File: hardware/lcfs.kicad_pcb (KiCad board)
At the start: 2 copper layers, 10 parts, among them J1 Pin_1x3, J2 Pin_1x3, J3 Pin_1x2_Battery, J4 Pin_1x3_Transmitter

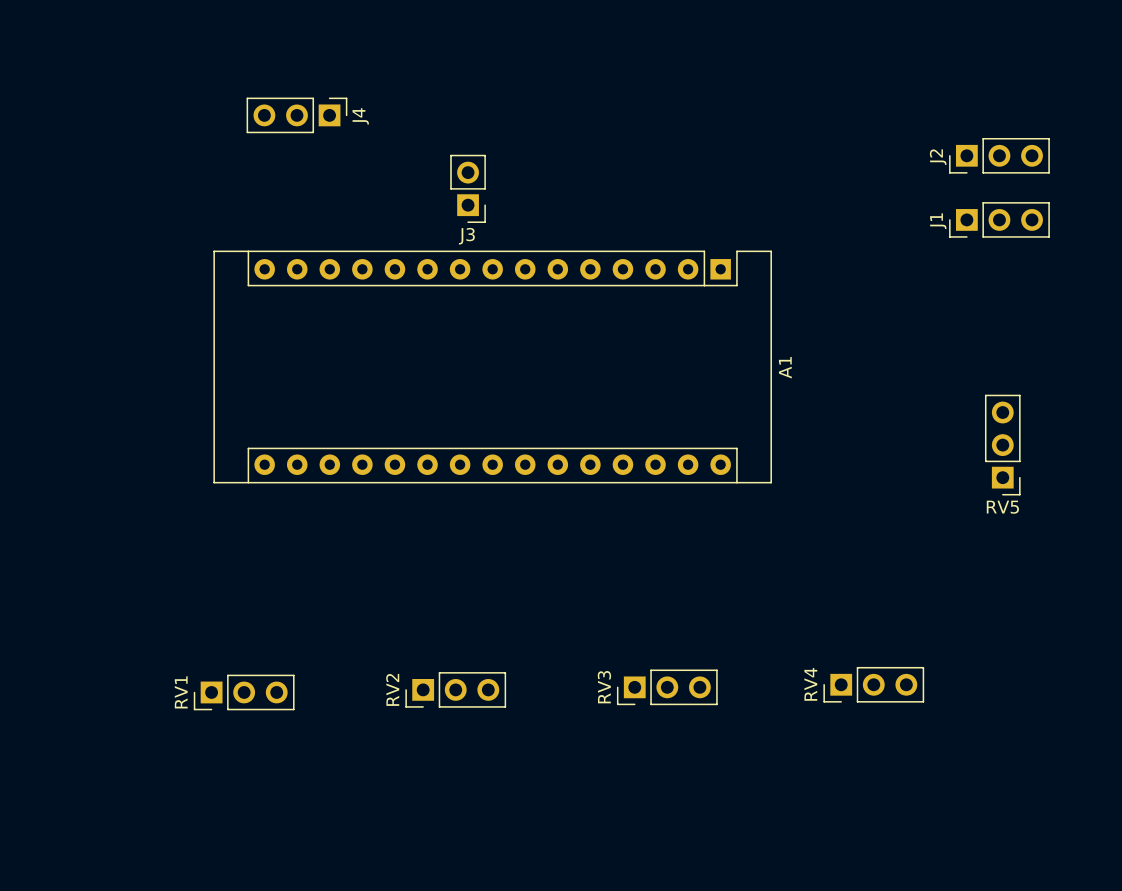
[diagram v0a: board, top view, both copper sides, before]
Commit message: v0.1.12 Posicionamento dos componentes na PCB
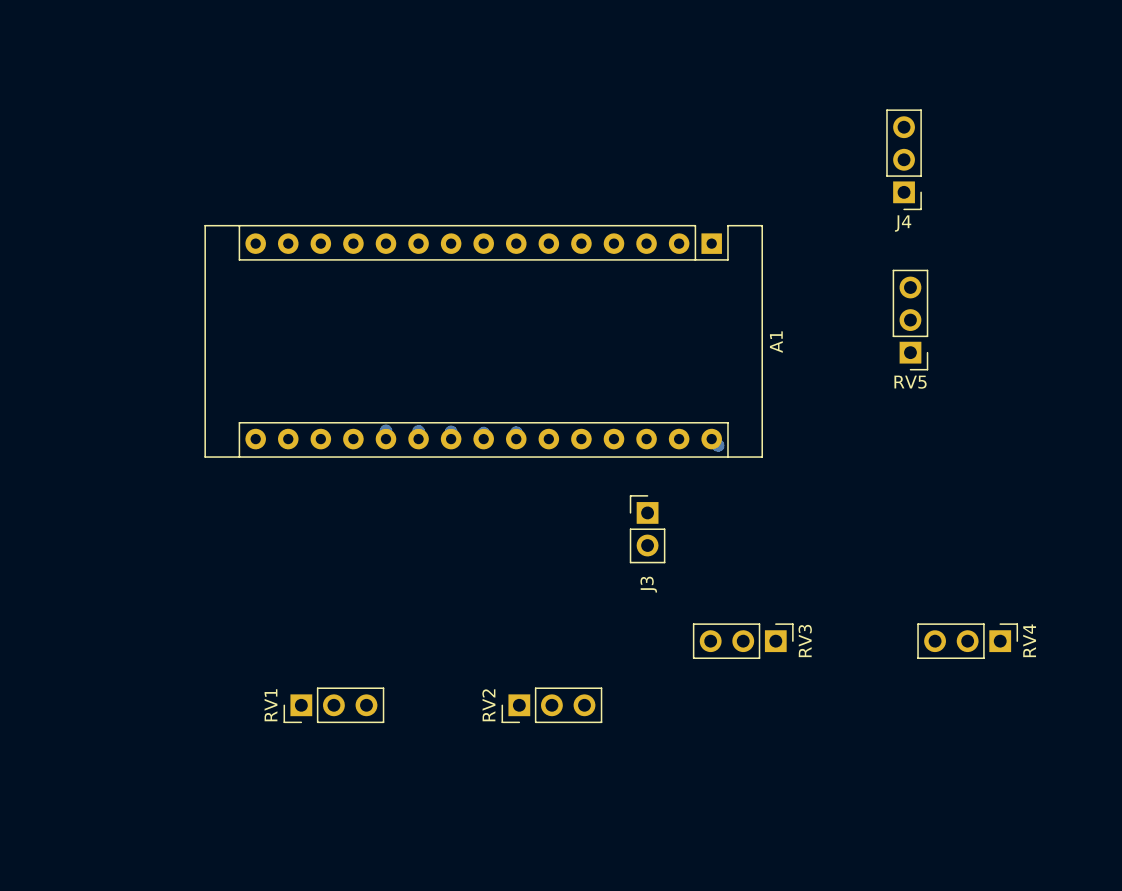
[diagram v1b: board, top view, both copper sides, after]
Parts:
- removed J1, J2: Pin_1x3, Socket_Strips:Socket_Strip_Straight_1x03_Pitch2.54mm
- moved J4 45.2 mm to (234.0, 121.0), turned to 180 degrees
- moved J3 27.8 mm to (214.0, 146.0), turned to 0 degrees
- moved RV4 12.9 mm to (241.5, 156.0), turned to 270 degrees
- moved RV5 12.1 mm to (234.5, 133.5)
- moved RV3 11.6 mm to (224.0, 156.0), turned to 270 degrees
- moved RV2 7.60 mm to (204.0, 161.0)
- moved RV1 7.07 mm to (187.0, 161.0)
- moved A1 2.12 mm to (219.0, 125.0)
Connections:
- A1 pad 30: Net-(A1-Pad30) -> /7.2V
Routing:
- net Net-(A1-Pad23): track 0.00 -> 0.77 mm
- net /7.2V: track 0.00 -> 0.71 mm
- net Net-(A1-Pad21): track 0.00 -> 0.70 mm
- net Net-(A1-Pad20): track 0.00 -> 0.64 mm
- net Net-(A1-Pad22): track 0.00 -> 0.62 mm
- net Net-(A1-Pad24): track 0.00 -> 0.50 mm
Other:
- net class Default: trace_width 0.25 -> 1
- board text added: "Battery"
- board text removed: "Battery 47mm x 10 mm"

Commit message: v0.1.13 PCB organizada e não preenchida
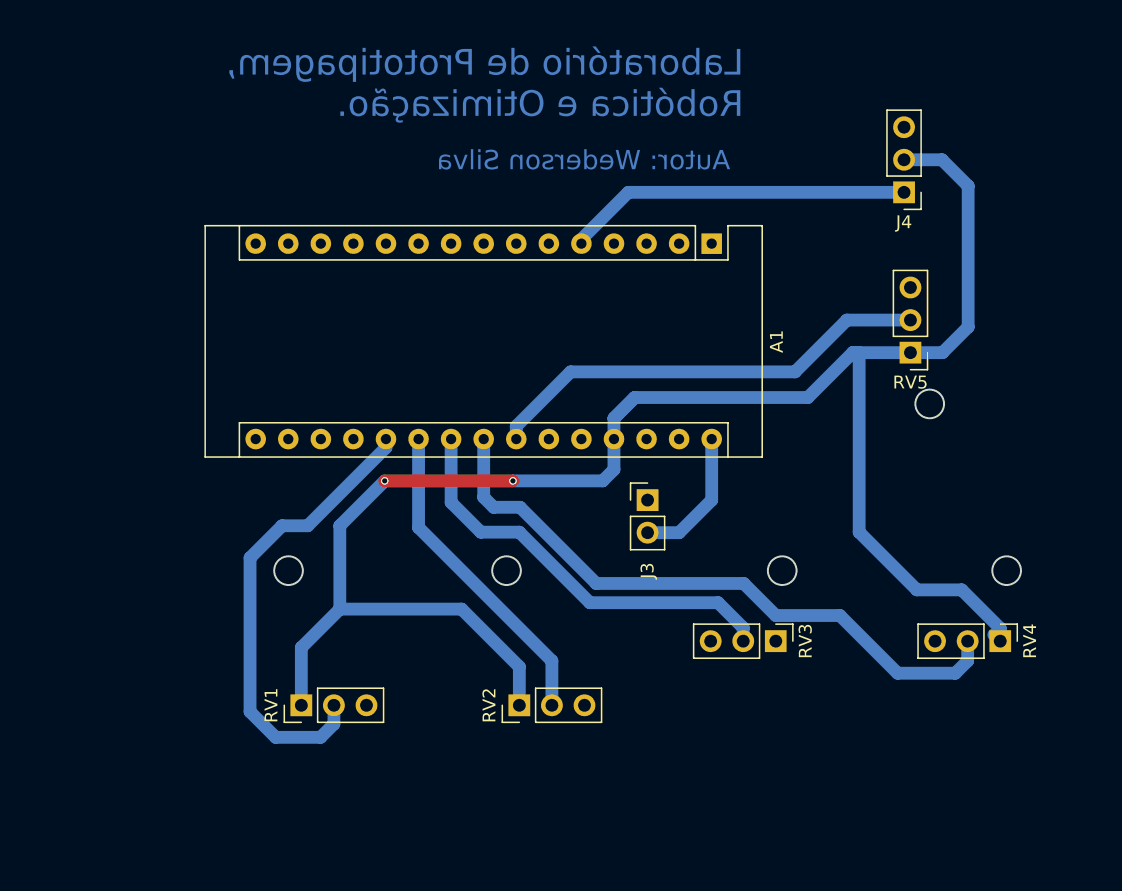
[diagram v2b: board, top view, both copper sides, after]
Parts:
- moved J3 1.00 mm to (214.0, 145.0)
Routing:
- net /5V: track 0.00 -> 141.3 mm, vias 0 -> 2
- net Net-(A1-Pad23): track 0.77 -> 49.9 mm
- net Net-(A1-Pad20): track 0.64 -> 36.1 mm
- net Net-(A1-Pad24): track 0.50 -> 35.2 mm
- net Net-(A1-Pad22): track 0.62 -> 32.9 mm
- net /DATA: track 0.00 -> 27.0 mm
- net Net-(A1-Pad21): track 0.70 -> 25.2 mm
- net /7.2V: track 0.71 -> 10.8 mm
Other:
- board outline added: 58.2 x 15.2 mm
- board text added: "Autor: Wederson Silva"
- board text added: "Laboratório de Prototipagem, Robótica e Otimização."

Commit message: v0.1.14 PCB preenchida e inclusão da pasta pictures
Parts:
- moved A1 7.50 mm to (219.0, 132.5)
- moved J3 7.50 mm to (214.0, 152.5)
- moved J4 7.50 mm to (234.0, 128.5)
- moved RV1 7.50 mm to (187.0, 168.5)
- moved RV2 7.50 mm to (204.0, 168.5)
- moved RV3 7.50 mm to (224.0, 163.5)
- moved RV4 7.50 mm to (241.5, 163.5)
- moved RV5 7.50 mm to (234.5, 141.0)
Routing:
- net /5V: track 141.3 -> 163.4 mm
- added copper zone on B.Cu, net /GND

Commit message: v0.1.15 Renomeia valores
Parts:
- moved A1 7.50 mm to (219.0, 125.0)
- moved J3 7.50 mm to (214.0, 145.0)
- moved J4 7.50 mm to (234.0, 121.0)
- moved RV1 7.50 mm to (187.0, 161.0)
- moved RV2 7.50 mm to (204.0, 161.0)
- moved RV3 7.50 mm to (224.0, 156.0)
- moved RV4 7.50 mm to (241.5, 156.0)
- moved RV5 7.50 mm to (234.5, 133.5)

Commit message: Inclui prints e fotos da PCB no Cap 3
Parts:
- J4: value Pin_1x3_Transmitter -> Pin_1x3_Transmissor
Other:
- board text added: "Bateria"
- board text removed: "Battery"
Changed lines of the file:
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@@
-(kicad_pcb (version 4) (host pcbnew 4.0.7)
+(kicad_pcb (version 20171130) (host pcbnew 5.0.0)
   (general
-    (links 21)
-    (no_connects 1)
-    (area 176.614999 113.8 251.61315 175.61315)
     (thickness 1.6)
     (drawings 31)
@@
       (layerselection 0x00030_80000001)
       (usegerberextensions false)
+      (usegerberattributes false)
+      (usegerberadvancedattributes false)
+      (creategerberjobfile false)
       (excludeedgelayer true)
       (linewidth 0.100000)
@@
       (hpglpennumber 1)
       (hpglpenspeed 20)
-      (hpglpendiameter 15)
-      (hpglpenoverlay 2)
+      (hpglpendiameter 15.000000)
       (psnegative false)
       (psa4output false)
@@
       (effects (font (size 1 1) (thickness 0.15)))
     )
-    (fp_text value Arduino_Nano (at 8.89 19.05 360) (layer F.Fab)
-      (effects (font (size 1 1) (thickness 0.15)))
-    )
-    (fp_text user %R (at 6.35 19.05 360) (layer F.Fab)
+    (fp_text value Arduino_Nano (at 7.8 19.05) (layer F.Fab)
+      (effects (font (size 1 1) (thickness 0.15)))
+    )
+    (fp_text user %R (at 4.6 19.05) (layer F.Fab)
       (effects (font (size 1 1) (thickness 0.15)))
     )
@@
       (effects (font (size 1 1) (thickness 0.15)))
     )
-    (fp_text value Pin_1x2_Battery (at 3 1 90) (layer F.Fab)
+    (fp_text value Pin_1x2_Battery (at -0.2 -2.4 180) (layer F.Fab)
       (effects (font (size 1 1) (thickness 0.15)))
     )
@@
       (net 28 /7.2V))
     (model ${KISYS3DMOD}/Socket_Strips.3dshapes/Socket_Strip_Straight_1x02_Pitch2.54mm.wrl
-      (at (xyz 0 -0.05 0))
+      (offset (xyz 0 -1.269999980926514 0))
       (scale (xyz 1 1 1))
       (rotate (xyz 0 0 270))
@@
       (effects (font (size 1 1) (thickness 0.15)))
     )
-    (fp_text value Pin_1x3_Transmitter (at 4 2.5 270) (layer F.Fab)
+    (fp_text value Pin_1x3_Transmissor (at 4 2.5 270) (layer F.Fab)
       (effects (font (size 1 1) (thickness 0.15)))
     )
@@
       (net 7 /GND))
     (model ${KISYS3DMOD}/Socket_Strips.3dshapes/Socket_Strip_Straight_1x03_Pitch2.54mm.wrl
-      (at (xyz 0 -0.1 0))
+      (offset (xyz 0 -2.539999961853027 0))
       (scale (xyz 1 1 1))
       (rotate (xyz 0 0 270))
@@
       (net 7 /GND))
     (model ${KISYS3DMOD}/Socket_Strips.3dshapes/Socket_Strip_Straight_1x03_Pitch2.54mm.wrl
-      (at (xyz 0 -0.1 0))
+      (offset (xyz 0 -2.539999961853027 0))
       (scale (xyz 1 1 1))
       (rotate (xyz 0 0 270))
@@
       (net 7 /GND))
     (model ${KISYS3DMOD}/Socket_Strips.3dshapes/Socket_Strip_Straight_1x03_Pitch2.54mm.wrl
-      (at (xyz 0 -0.1 0))
+      (offset (xyz 0 -2.539999961853027 0))
       (scale (xyz 1 1 1))
       (rotate (xyz 0 0 270))
@@
       (effects (font (size 1 1) (thickness 0.15)))
     )
-    (fp_text value "POT 3" (at 3 2.5 360) (layer F.Fab)
+    (fp_text value "POT 3" (at 3 2.5) (layer F.Fab)
       (effects (font (size 1 1) (thickness 0.15)))
     )
@@
       (net 7 /GND))
     (model ${KISYS3DMOD}/Socket_Strips.3dshapes/Socket_Strip_Straight_1x03_Pitch2.54mm.wrl
-      (at (xyz 0 -0.1 0))
+      (offset (xyz 0 -2.539999961853027 0))
       (scale (xyz 1 1 1))
       (rotate (xyz 0 0 270))
@@
       (effects (font (size 1 1) (thickness 0.15)))
     )
-    (fp_text value "POT 4" (at 6.5 2.5 360) (layer F.Fab)
+    (fp_text value "POT 4" (at 6.5 2.5) (layer F.Fab)
       (effects (font (size 1 1) (thickness 0.15)))
     )
@@
       (net 7 /GND))
     (model ${KISYS3DMOD}/Socket_Strips.3dshapes/Socket_Strip_Straight_1x03_Pitch2.54mm.wrl
-      (at (xyz 0 -0.1 0))
+      (offset (xyz 0 -2.539999961853027 0))
       (scale (xyz 1 1 1))
       (rotate (xyz 0 0 270))
@@
       (net 7 /GND))
     (model ${KISYS3DMOD}/Socket_Strips.3dshapes/Socket_Strip_Straight_1x03_Pitch2.54mm.wrl
-      (at (xyz 0 -0.1 0))
+      (offset (xyz 0 -2.539999961853027 0))
       (scale (xyz 1 1 1))
       (rotate (xyz 0 0 270))
@@
   (gr_line (start 224.5 128) (end 231.5 128) (angle 90) (layer Eco2.User) (width 0.2))
   (gr_line (start 224.5 109) (end 224.5 128) (angle 90) (layer Eco2.User) (width 0.2))
-  (gr_text Battery (at 199 107.5) (layer Eco2.User)
+  (gr_text Bateria (at 199 107.5) (layer Eco2.User)
     (effects (font (size 1.5 1.5) (thickness 0.3)))
   )
